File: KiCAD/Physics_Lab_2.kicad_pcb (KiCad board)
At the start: 2 copper layers, 58.5 x 57 mm, 13 parts, among them J1 USB_C, U1 MCP73871, U2 S2B-PH-K-S-GW

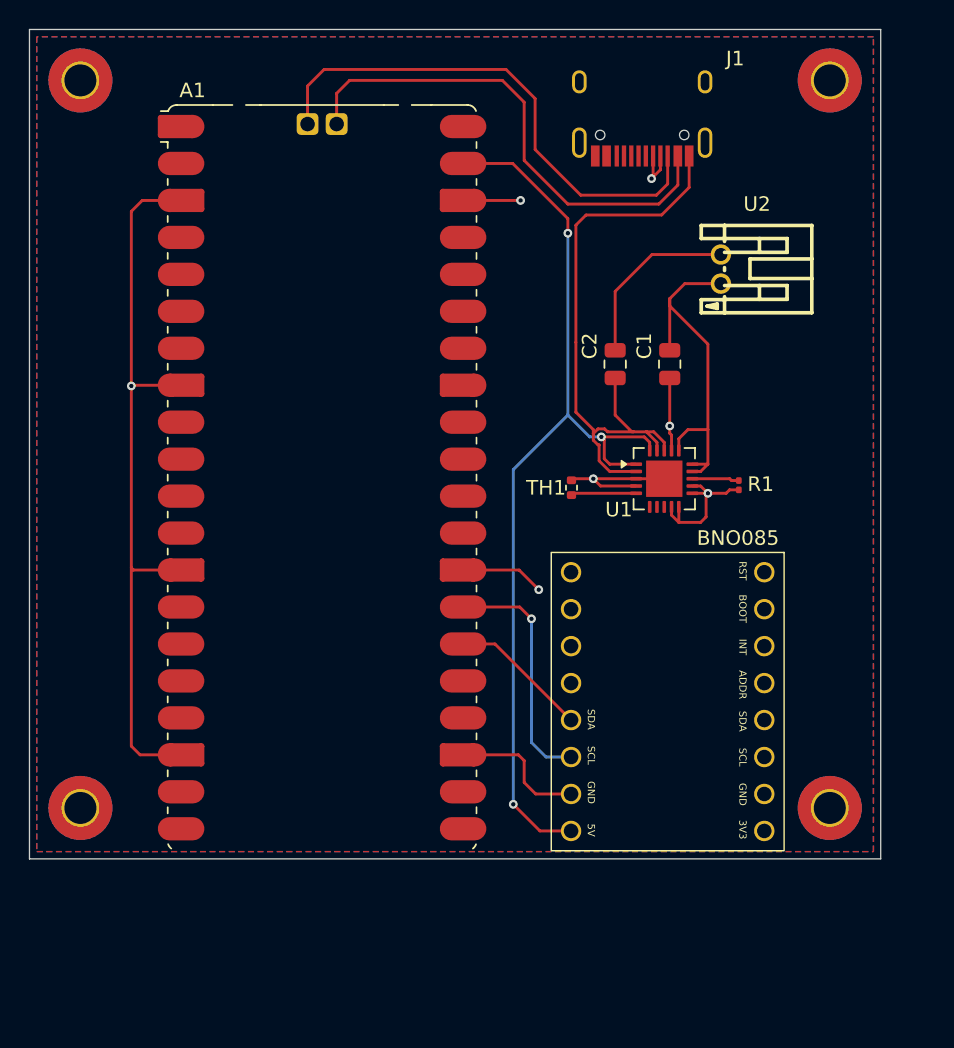
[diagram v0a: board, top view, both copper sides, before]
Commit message: Fix merge conflict by pause
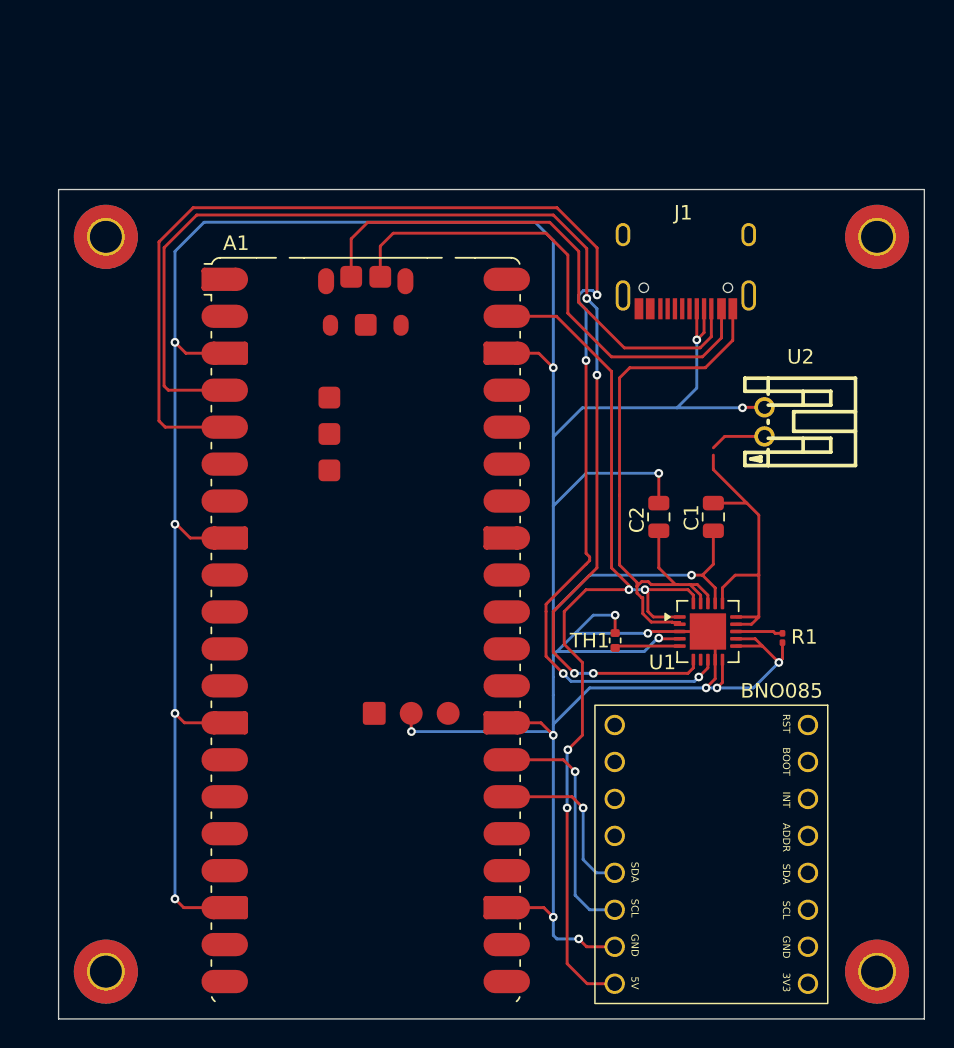
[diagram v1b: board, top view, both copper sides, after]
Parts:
- removed the REF** at (155.0, 53.5)
- removed the REF** at (155.0, 103.5)
- removed the REF** at (103.5, 103.5)
- removed the REF** at (103.5, 53.5)
- added REF**: MountingHole_2.2mm_M2_Pad_TopBottom, MountingHole:MountingHole_2.2mm_M2_Pad_TopBottom, F.Cu at (158.2, 64.2)
- added REF**: MountingHole_2.2mm_M2_Pad_TopBottom, MountingHole:MountingHole_2.2mm_M2_Pad_TopBottom, F.Cu at (105.2, 64.2)
- added REF**: MountingHole_2.2mm_M2_Pad_TopBottom, MountingHole:MountingHole_2.2mm_M2_Pad_TopBottom, F.Cu at (105.2, 114.8)
- added REF**: MountingHole_2.2mm_M2_Pad_TopBottom, MountingHole:MountingHole_2.2mm_M2_Pad_TopBottom, F.Cu at (158.2, 114.8)
- moved A1 10.9 mm to (123.1, 91.3)
- moved BNO085_Halley1 10.9 mm to (153.5, 97.8)
- moved C1 10.9 mm to (147.0, 83.5)
- moved C2 10.9 mm to (143.2, 83.5)
- moved J1 10.9 mm to (145.1, 61.5)
- moved R1 10.9 mm to (151.8, 91.8)
- moved TH1 10.9 mm to (140.2, 92.0)
- moved U1 10.9 mm to (146.6, 91.4)
- moved U2 10.9 mm to (150.5, 77.0)
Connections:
- A1 pad 4: unconnected-(A1-GPIO2-Pad4) -> Net-(A1-GPIO2)
- A1 pad 5: unconnected-(A1-GPIO3-Pad5) -> Net-(A1-GPIO3)
- C1 pad 1: Net-(U1-V_{BAT_SENSE}) -> +5V
- U1 pad 14: Net-(U1-V_{BAT_SENSE}) -> +5V
- U1 pad 15: Net-(U1-V_{BAT_SENSE}) -> +5V
- U1 pad 16: Net-(U1-V_{BAT_SENSE}) -> +5V
- U1 pad 6: unconnected-(U1-~{PG}-Pad6) -> Net-(A1-GPIO2)
- U1 pad 8: unconnected-(U1-STAT1/~{LBO}-Pad8) -> Net-(A1-GPIO3)
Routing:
- net GND: track 111.4 -> 268.7 mm, vias 7 -> 19
- net Net-(A1-GPIO3): track 0.00 -> 93.1 mm, vias 0 -> 4
- net Net-(A1-GPIO2): track 0.00 -> 85.0 mm, vias 0 -> 4
- net +5V: track 0.00 -> 21.6 mm
- net Net-(U1-V_{BAT_SENSE}): track 25.4 -> 3.84 mm
- net Net-(A1-GPIO20): track 9.86 -> 11.9 mm, vias 0 -> 1
- net Net-(A1-VSYS): track 66.5 -> 67.7 mm, vias 3 -> 4
- removed copper zone on B.Cu, net GND
- removed copper zone on F.Cu, net GND
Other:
- board size 58.5 x 57 mm -> 59.5 x 57 mm

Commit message: Fix wiring to battery and grounding
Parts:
- removed the REF** at (158.2, 64.2)
- removed the REF** at (105.2, 64.2)
- removed the REF** at (105.2, 114.8)
- removed the REF** at (158.2, 114.8)
- added REF**: MountingHole_2.2mm_M2_DIN965_Pad, MountingHole:MountingHole_2.2mm_M2_DIN965_Pad, F.Cu at (105.0, 65.0)
- added REF**: MountingHole_2.2mm_M2_DIN965_Pad, MountingHole:MountingHole_2.2mm_M2_DIN965_Pad, F.Cu at (158.2, 114.8)
- added REF**: MountingHole_2.2mm_M2_DIN965_Pad, MountingHole:MountingHole_2.2mm_M2_DIN965_Pad, F.Cu at (158.2, 65.0)
- added REF**: MountingHole_2.2mm_M2_DIN965_Pad, MountingHole:MountingHole_2.2mm_M2_DIN965_Pad, F.Cu at (105.2, 114.8)
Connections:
- C1 pad 1: +5V -> Net-(U1-V_{BAT_SENSE})
- U1 pad 14: +5V -> Net-(U1-V_{BAT_SENSE})
- U1 pad 15: +5V -> Net-(U1-V_{BAT_SENSE})
- U1 pad 16: +5V -> Net-(U1-V_{BAT_SENSE})
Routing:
- net GND: track 268.7 -> 326.6 mm
- net Net-(U1-V_{BAT_SENSE}): track 3.84 -> 25.7 mm, vias 0 -> 1
- net +5V: track 21.6 -> 0.00 mm

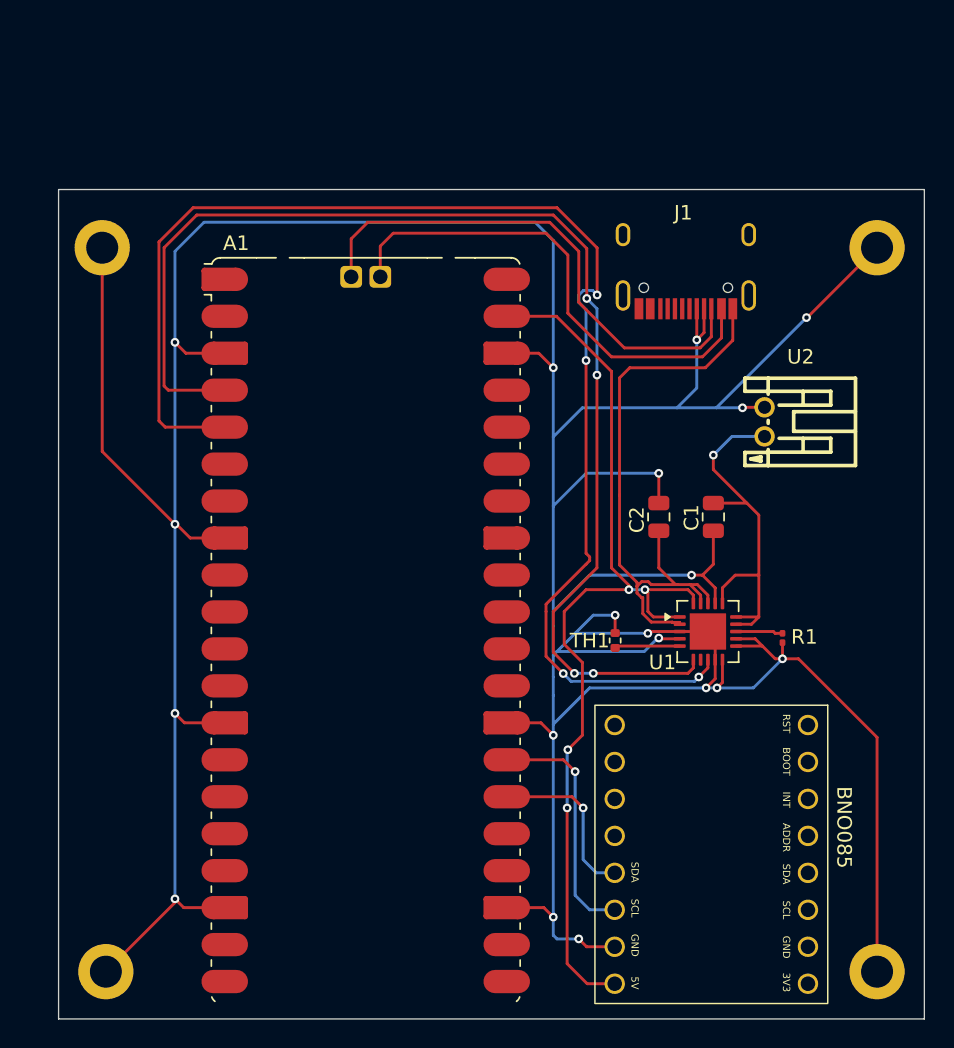
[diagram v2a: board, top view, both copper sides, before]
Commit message: Add ordering placeholder text
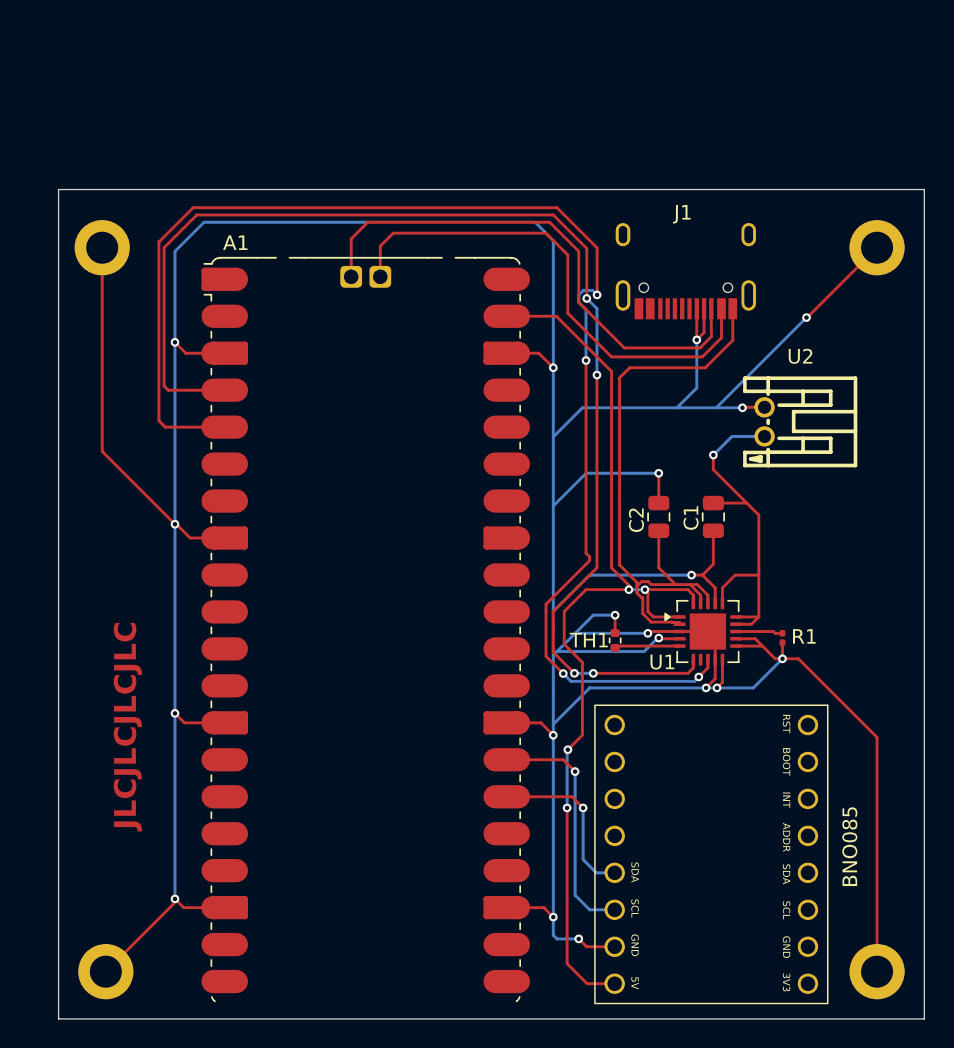
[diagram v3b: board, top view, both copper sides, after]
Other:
- board text added: "JLCJLCJLCJLC"
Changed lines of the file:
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@@
 			)
 		)
+		(property "LCSC" "C165948"
+			(at 0 0 0)
+			(layer "F.SilkS")
+			(hide yes)
+			(effects
+				(font
+					(size 1.27 1.27)
+					(thickness 0.15)
+				)
+			)
+		)
 		(property ki_fp_filters "USB*")
 		(sheetname "/")
@@
 		(tags "resistor")
 		(property "Reference" "TH1"
-			(at 0.01 1.75 180)
+			(at 0.01 1.75 0)
 			(layer "F.SilkS")
 			(effects
@@
 			)
 		)
+		(property "LCSC" "C25531"
+			(at 0 0 0)
+			(layer "F.SilkS")
+			(hide yes)
+			(effects
+				(font
+					(size 1.27 1.27)
+					(thickness 0.15)
+				)
+			)
+		)
 		(property ki_fp_filters "R_* RV_*")
 		(sheetname "/")
@@
 		)
 		(fp_text user "BNO085"
-			(at 4.2 -1.9 270)
+			(at 11.2 -3.5 90)
 			(unlocked yes)
 			(layer "F.SilkS")
@@
 			)
 		)
+		(property "LCSC" "C100158"
+			(at 0 0 0)
+			(layer "F.SilkS")
+			(hide yes)
+			(effects
+				(font
+					(size 1.27 1.27)
+					(thickness 0.15)
+				)
+			)
+		)
 		(property ki_fp_filters "R_*")
 		(sheetname "/")
@@
 			)
 		)
+		(property "LCSC" "C1779"
+			(at 0 0 0)
+			(layer "F.SilkS")
+			(hide yes)
+			(effects
+				(font
+					(size 1.27 1.27)
+					(thickness 0.15)
+				)
+			)
+		)
 		(property ki_fp_filters "C_*")
 		(sheetname "/")
@@
 			)
 		)
+		(property "LCSC" "C1713"
+			(at 0 0 0)
+			(layer "F.SilkS")
+			(hide yes)
+			(effects
+				(font
+					(size 1.27 1.27)
+					(thickness 0.15)
+				)
+			)
+		)
 		(property ki_fp_filters "C_*")
 		(sheetname "/")
@@
 			)
 		)
+		(property "LCSC" "C185603"
+			(at 0 0 0)
+			(layer "F.SilkS")
+			(hide yes)
+			(effects
+				(font
+					(size 1.27 1.27)
+					(thickness 0.15)
+				)
+			)
+		)
 		(property ki_fp_filters "QFN*4x4mm*P0.5mm*")
 		(sheetname "/")
@@
 		(sheetname "/")
 		(sheetfile "Physics_Lab_2.kicad_sch")
-		(attr smd)
+		(attr smd exclude_from_pos_files exclude_from_bom)
 		(fp_line
 			(start -10.61 -23.07)
@@
 		(layer "Edge.Cuts")
 	)
+	(gr_text "JLCJLCJLCJLC"
+		(at 107.5 105 90)
+		(layer "F.Cu")
+		(effects
+			(font
+				(size 1.5 1.5)
+				(thickness 0.3)
+				(bold yes)
+			)
+			(justify left bottom)
+		)
+	)
 	(segment
